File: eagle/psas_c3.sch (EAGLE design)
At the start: 4 parts, among them IC1 MCP73871, U1 MIC5219 3.3V

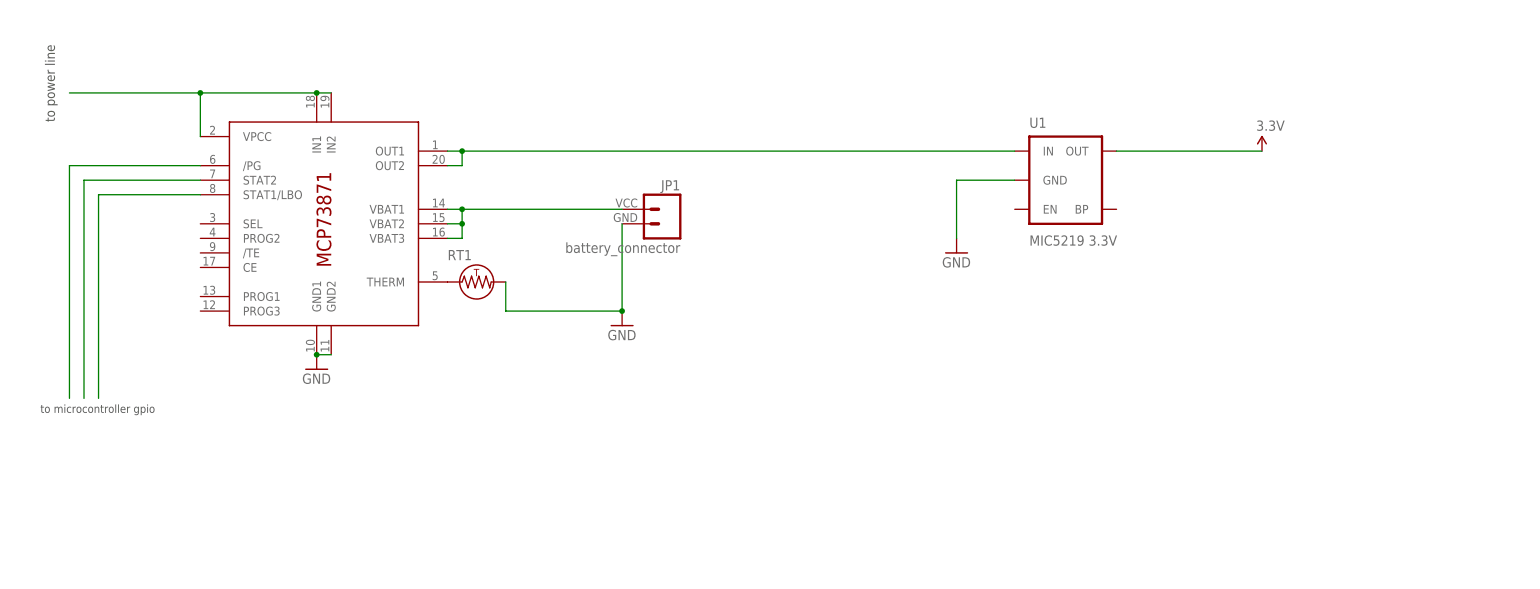
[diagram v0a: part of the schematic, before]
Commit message: touched up the battery charger and voltage regulator circuit
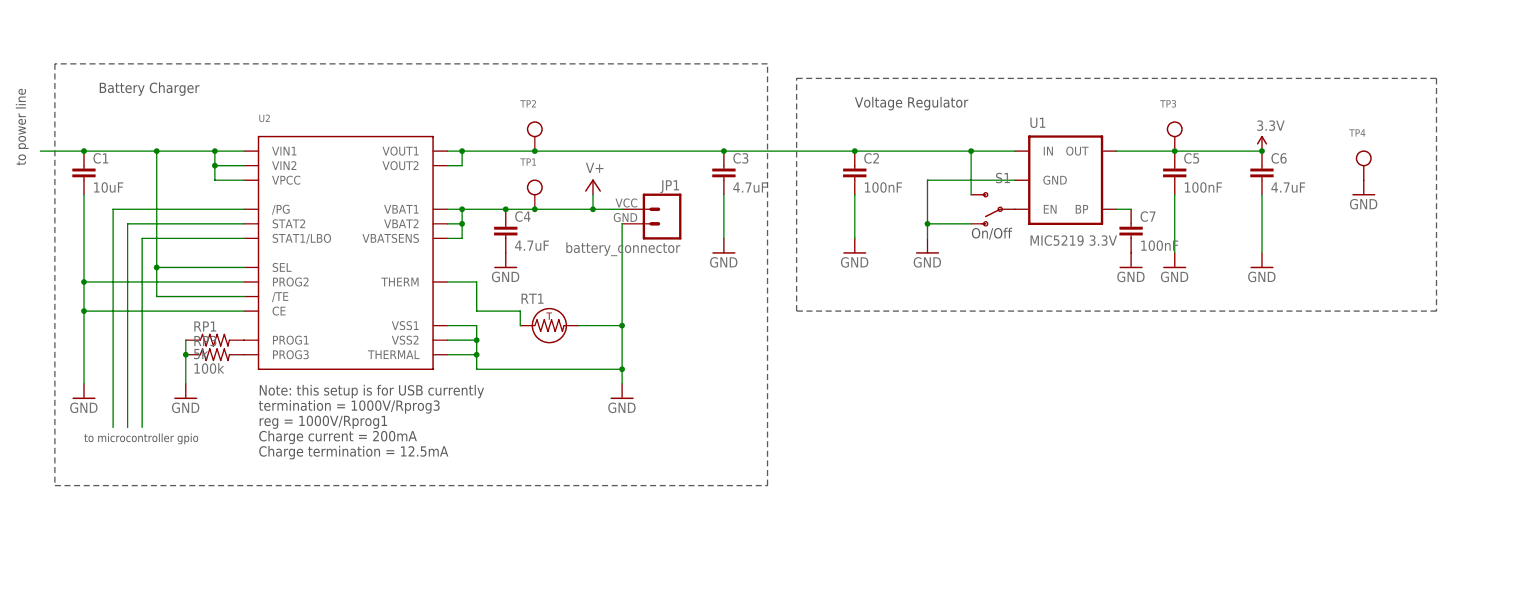
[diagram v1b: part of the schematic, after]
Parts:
- removed IC1: MCP73871, Vibrogait_prototype:MCP73871
- added C1: 10uF, rcl_custom:C-EU0603-B-NOSILK
- added C2, C5, C7: 100nF, rcl_custom:C-EU0603-B-NOSILK
- added C3, C4, C6: 4.7uF, rcl_custom:C-EU0603-B-NOSILK
- added RP1: 5k, rcl_custom:R-US_0603-B-NOSILK
- added RP3: 100k, rcl_custom:R-US_0603-B-NOSILK
- added S1: (no value), Vibrogait_prototype:SWITCH-SPSTPTH
- added TP1, TP2, TP3, TP4: (no value), microbuilder:TESTPOINT0.1"
- added U2: (no value), microbuilder:MCP73871
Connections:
- new net N$10: RP3.2, U2.PROG3
- new net N$8: S1.P, U1.EN
- new net N$9: RP1.2, U2.PROG1
- new net V+: C4.1, JP1.2, TP1.P$1, U2.VBAT1, U2.VBAT2, U2.VBATSENS
- net 3.3V: now also C5.1, C6.1, TP3.P$1
- net GND: now also C1.2, C2.2, C3.2, C4.2, C5.2, C6.2, C7.2, RP1.1, RP3.1, S1.O, TP4.P$1, U2.CE, U2.PROG2, U2.THERMAL, U2.VSS1, U2.VSS2; no longer IC1.GND1, IC1.GND2
- net N$1: now also C7.1, U1.BP; no longer IC1.VBAT1, IC1.VBAT2, IC1.VBAT3, JP1.2
- net N$2: now also C2.1, C3.1, S1.S, TP2.P$1, U2.VOUT1, U2.VOUT2; no longer IC1.OUT1, IC1.OUT2
- net N$3: now also U2./PG; no longer IC1./PG
- net N$4: now also U2.STAT2; no longer IC1.STAT2
- net N$5: now also U2.STAT1/LBO; no longer IC1.STAT1/LBO
- net N$6: now also U2.THERM; no longer IC1.THERM
- net N$7: now also C1.1, U2./TE, U2.SEL, U2.VIN1, U2.VIN2, U2.VPCC; no longer IC1.IN1, IC1.IN2, IC1.VPCC
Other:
- note added: "Battery Charger"
- note added: "Note: this setup is for USB currently termination = 1000V/Rprog3 reg = 1000V/Rprog1 Charge current = 200mA Charge termination = 12.5mA"
- note added: "On/Off"
- note added: "Voltage Regulator"
- moved on the sheet: RT1

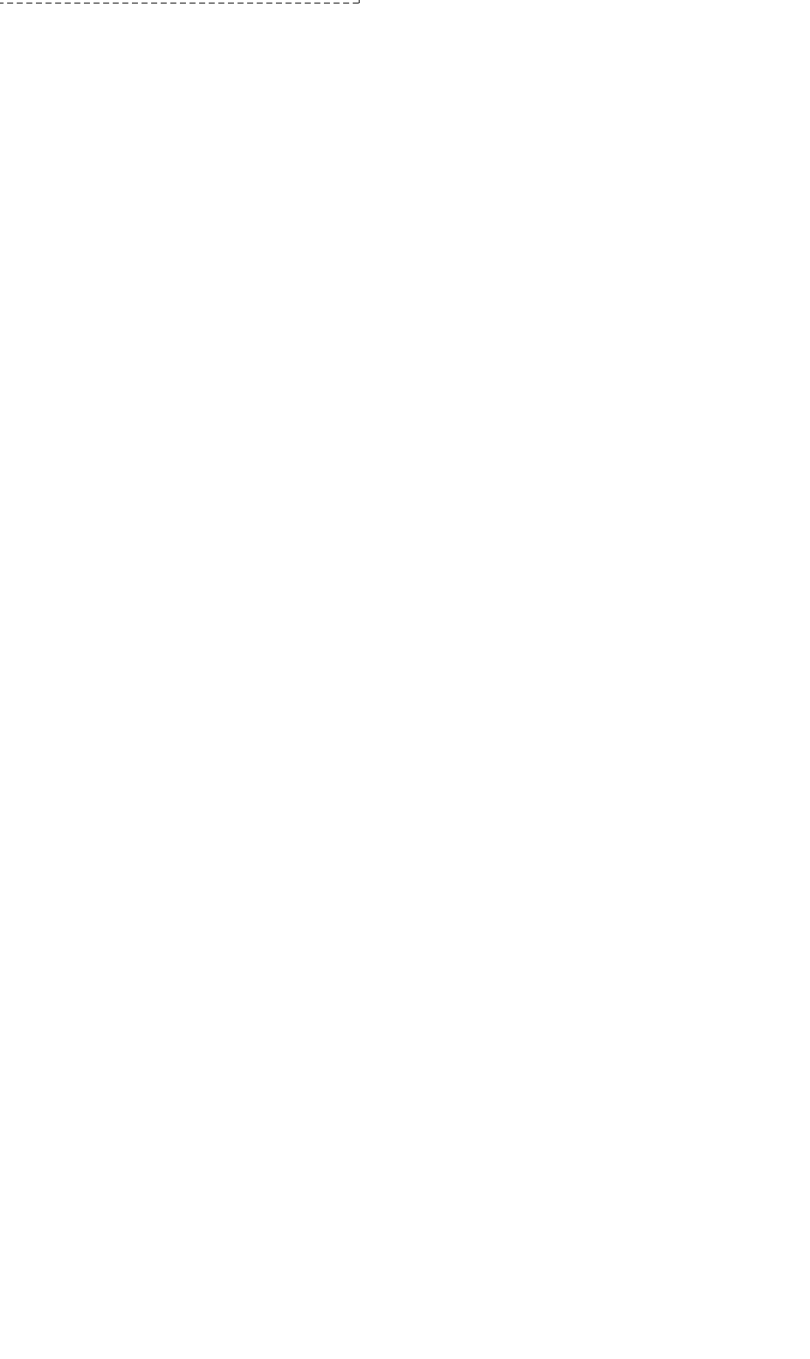
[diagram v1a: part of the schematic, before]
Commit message: added microcontroller unit to library and placed on sch/brd
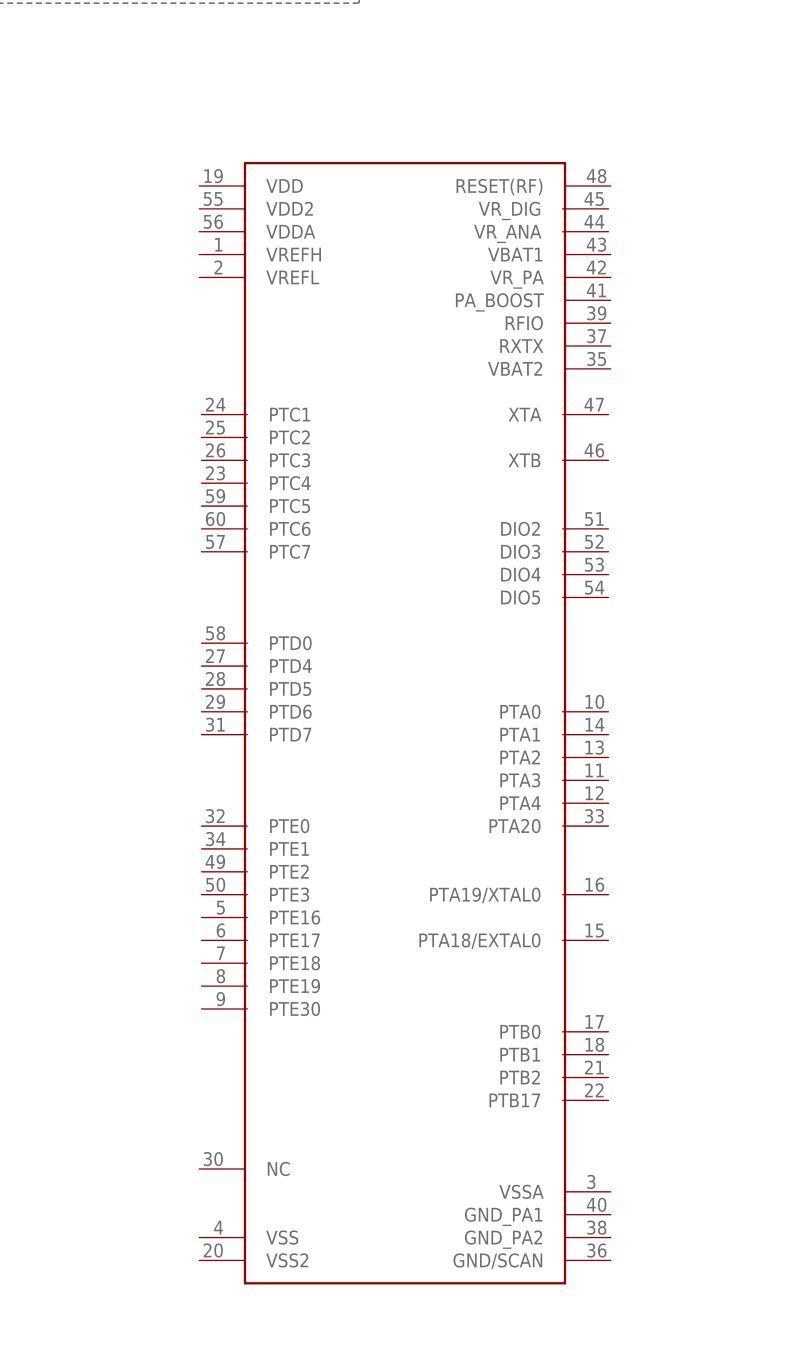
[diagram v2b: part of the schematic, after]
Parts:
- added U$1: MKW01Z128, psas_c3:MKW01Z128
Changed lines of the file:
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@@
 <part name="S1" library="Vibrogait_prototype" deviceset="SWITCH-SPST" device="PTH"/>
 <part name="GND11" library="Vibrogait_prototype" deviceset="GND" device=""/>
+<part name="U$1" library="psas_c3" deviceset="MKW01Z128" device=""/>
 </parts>
 <sheets>
@@
 <instance part="S1" gate="1" x="180.34" y="203.2" rot="R180"/>
 <instance part="GND11" gate="1" x="93.98" y="193.04"/>
+<instance part="U$1" gate="G$1" x="127" y="12.7"/>
 </instances>
 <busses>

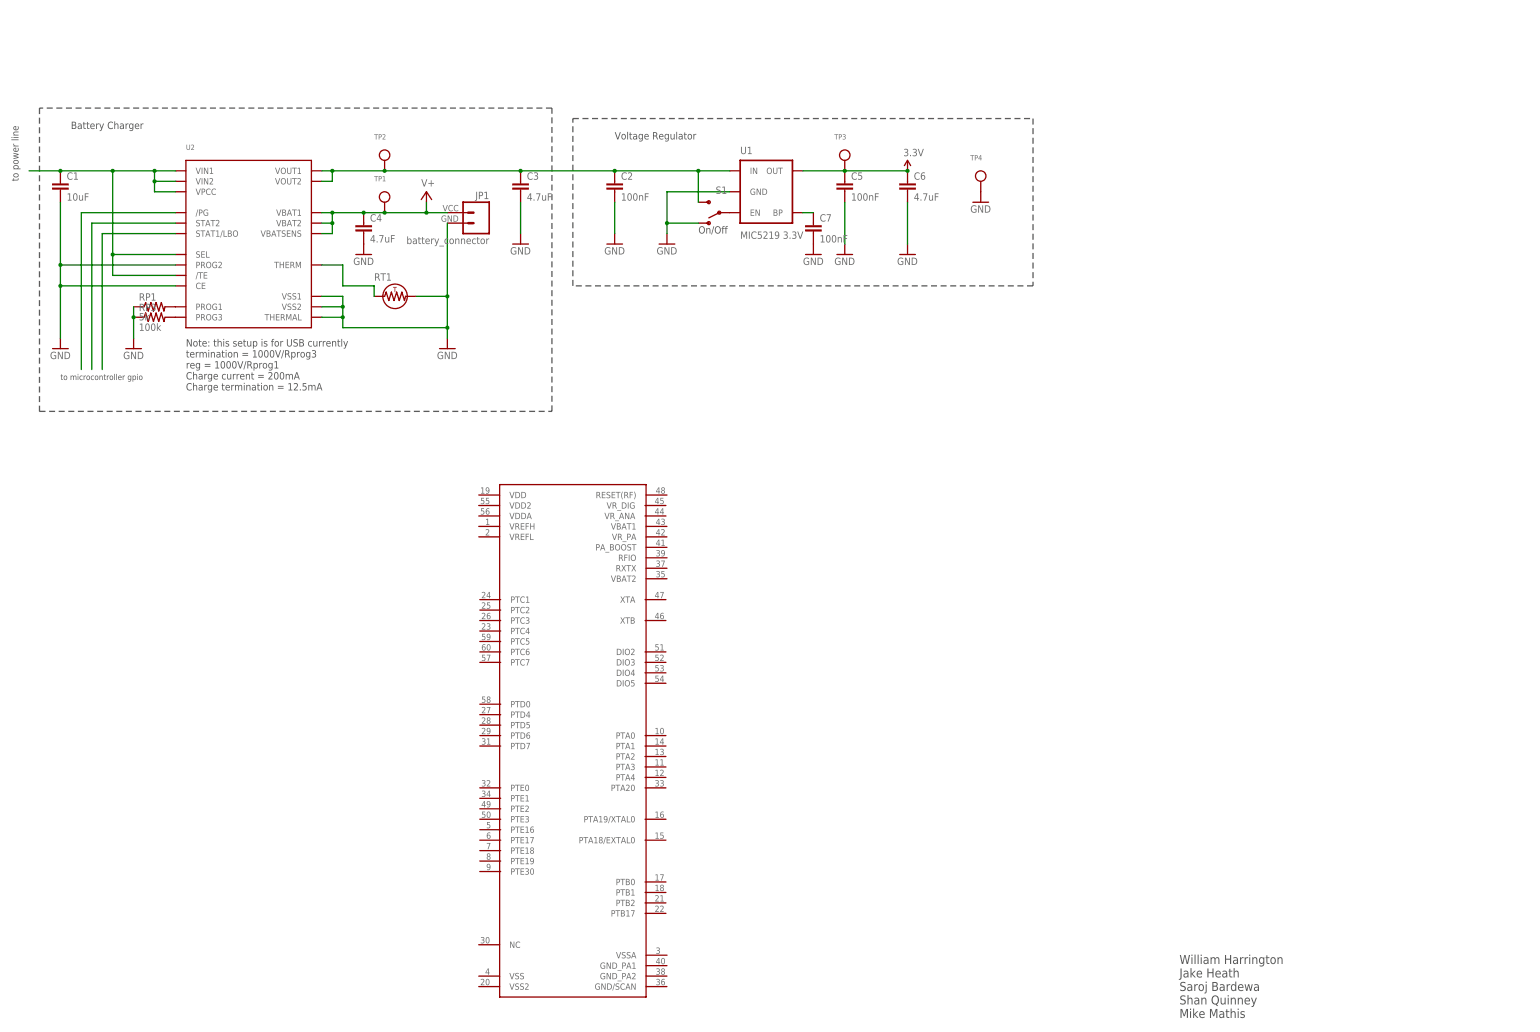
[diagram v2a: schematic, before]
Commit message: revised PDS, MCU is on schematic & board now along with new USB2UART chip (added datasheet for that as well)
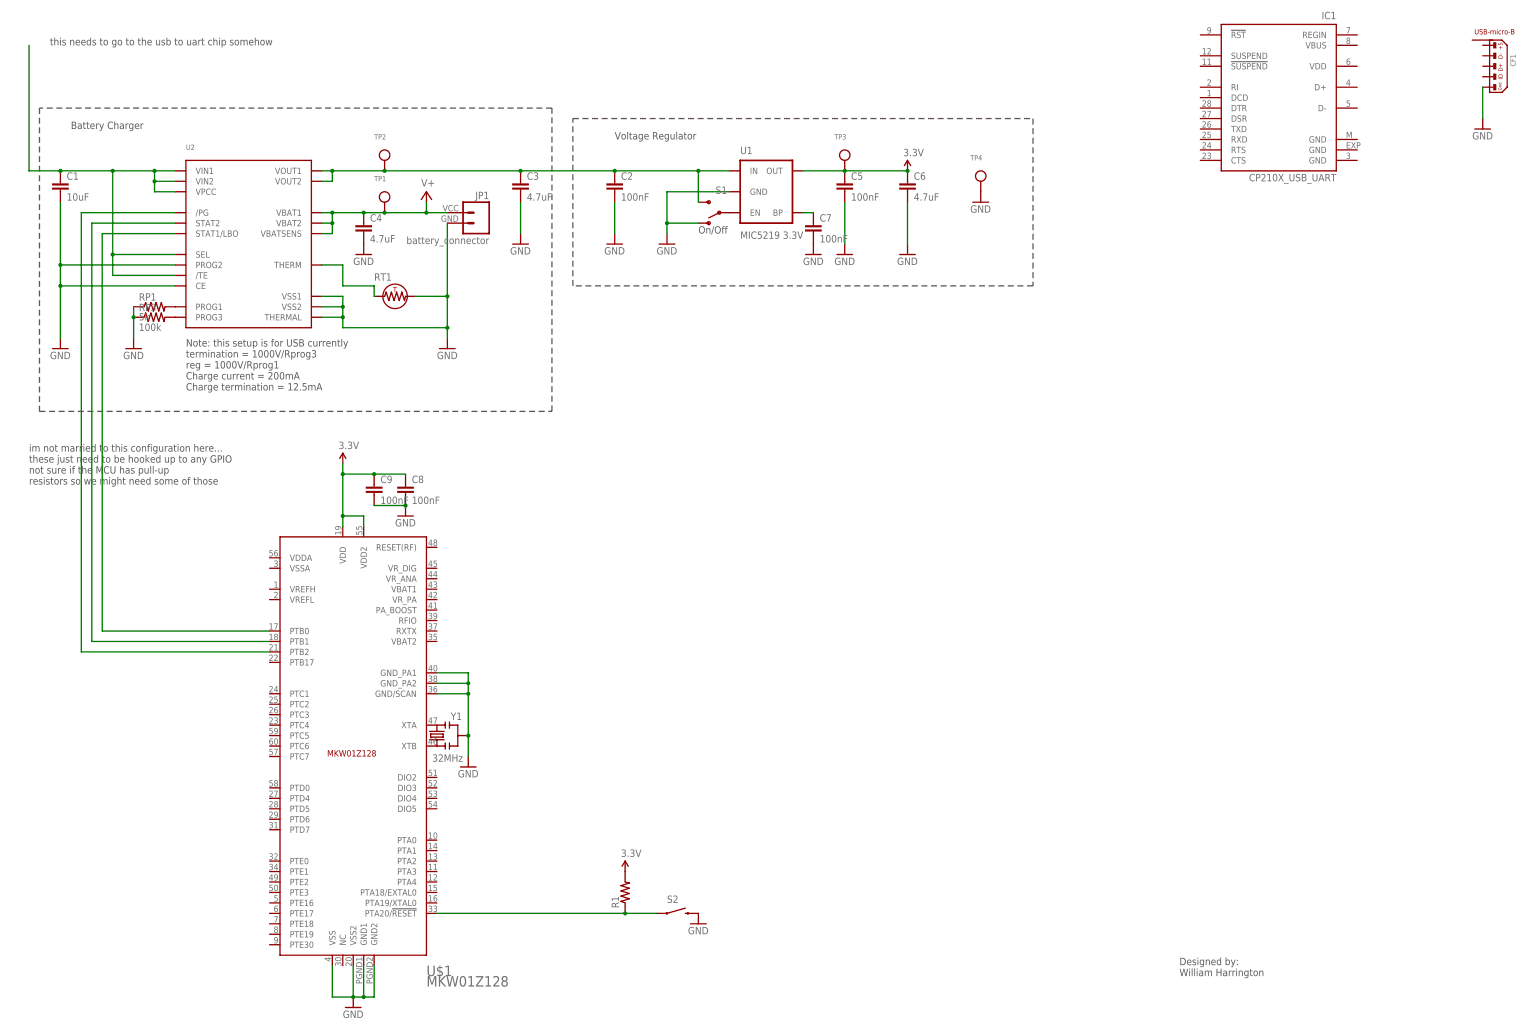
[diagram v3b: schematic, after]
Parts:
- added C8, C9: 100nF, Vibrogait_prototype:C-EU0603-B-NOSILK
- added CF1: (no value), Vibrogait_prototype:CON_USB-MICRO-B-RECEPTACLE-PTH-HIROSE-ZX62D-B-5P8
- added IC1: CP210X_USB_UART, SparkFun-v5:CP210X_USB_UART
- added R1: (no value), rcl_custom:R-US_0603-B-NOSILK
- added S2: SWITCH-MOMENTARY-2, Vibrogait_prototype:SWITCH-MOMENTARY-2
- added Y1: 32MHz, Lilypad_Arduino_USB_v12:SPARKFUN-FREQCTRL_RESONATOR16MHZ
- U$1: DIST (none) -> Digi-Key; DPN (none) -> MKW01Z128CHN-ND; MFN (none) -> Freescale Semiconductor; MPN (none) -> MKW01Z128CHN
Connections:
- new net N$11: U$1.XTB, Y1.1
- new net N$12: U$1.XTA, Y1.3
- new net N$13: R1.1, S2.1, U$1.PTA20/!RESET
- net 3.3V: now also C8.1, C9.1, R1.2, U$1.VDD, U$1.VDD2
- net GND: now also C8.2, C9.2, CF1.5, S2.2, U$1.GND/SCAN, U$1.GND1, U$1.GND2, U$1.GND_PA1, U$1.GND_PA2, U$1.VSS, U$1.VSS2, Y1.2
- net N$3: now also U$1.PTB2
- net N$4: now also U$1.PTB1
- net N$5: now also U$1.PTB0
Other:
- note added: "Designed by: William Harrington"
- note added: "im not married to this configuration here... these just need to be hooked up to any GPIO not sure if the MCU has pull-up resistors so we might need some of those"
- note added: "this needs to go to the usb to uart chip somehow"
- note removed: "William Harrington Jake Heath Saroj Bardewa Shan Quinney Mike Mathis"
- note removed: "to microcontroller gpio"
- note removed: "to power line"

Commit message: clock configuration
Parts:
- added JP2: (no value), SparkFun-v5:M02PTH
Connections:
- new net N$14: JP2.2, U$1.DIO5
- new net N$15: JP2.1, U$1.PTA18/EXTAL0
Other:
- note added: "clock selection: when jumper connects pins MCU runs off 32MHz clock with prescaler of 1.5 to obtain 48MHz, otherwise the MCU needs to run off internal clock reference (see datasheet for details)"
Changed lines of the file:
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@@
 <attribute name="MPN" value="CP2101-GM"/>
 </part>
+<part name="JP2" library="SparkFun-v5" deviceset="M02" device="PTH"/>
 </parts>
 <sheets>
@@
 not sure if the MCU has pull-up
 resistors so we might need some of those</text>
+<text x="177.8" y="50.8" size="1.778" layer="97">clock selection:
+when jumper connects pins
+MCU runs off 32MHz clock
+with prescaler of 1.5 to obtain
+48MHz, otherwise the MCU needs
+to run off internal clock reference
+(see datasheet for details)</text>
 </plain>
 <instances>
@@
 <attribute name="MPN" x="317.5" y="231.14" size="1.778" layer="96" rot="MR0" display="off"/>
 </instance>
+<instance part="JP2" gate="G$1" x="172.72" y="55.88" rot="MR0"/>
 </instances>
 <busses>
@@
 </segment>
 </net>
+<net name="N$14" class="0">
+<segment>
+<pinref part="U$1" gate="G$1" pin="DIO5"/>
+<pinref part="JP2" gate="G$1" pin="2"/>
+<wire x1="111.76" y1="58.42" x2="165.1" y2="58.42" width="0.1524" layer="91"/>
+</segment>
+</net>
+<net name="N$15" class="0">
+<segment>
+<pinref part="U$1" gate="G$1" pin="PTA18/EXTAL0"/>
+<pinref part="JP2" gate="G$1" pin="1"/>
+<wire x1="111.76" y1="38.1" x2="165.1" y2="38.1" width="0.1524" layer="91"/>
+<wire x1="165.1" y1="38.1" x2="165.1" y2="55.88" width="0.1524" layer="91"/>
+</segment>
+</net>
